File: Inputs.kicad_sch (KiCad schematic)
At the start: 12 parts, among them J7 Screw_Terminal_01x04, J8 Screw_Terminal_01x04, U10 LTV-247, U9 LTV-247

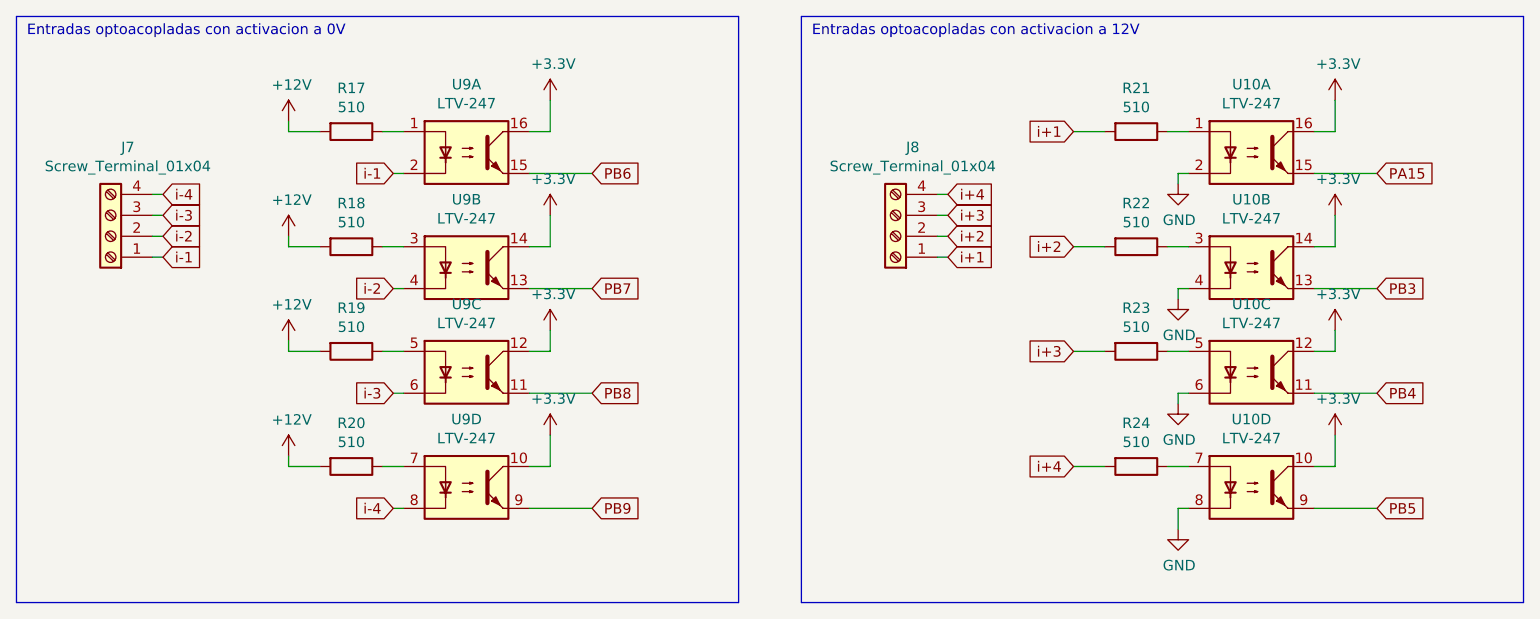
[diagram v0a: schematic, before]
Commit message: Planteamiento nuevo proeycto de mosquito - Se eelmiraon del esquematico las entradas a 0V y las salidas a Leds
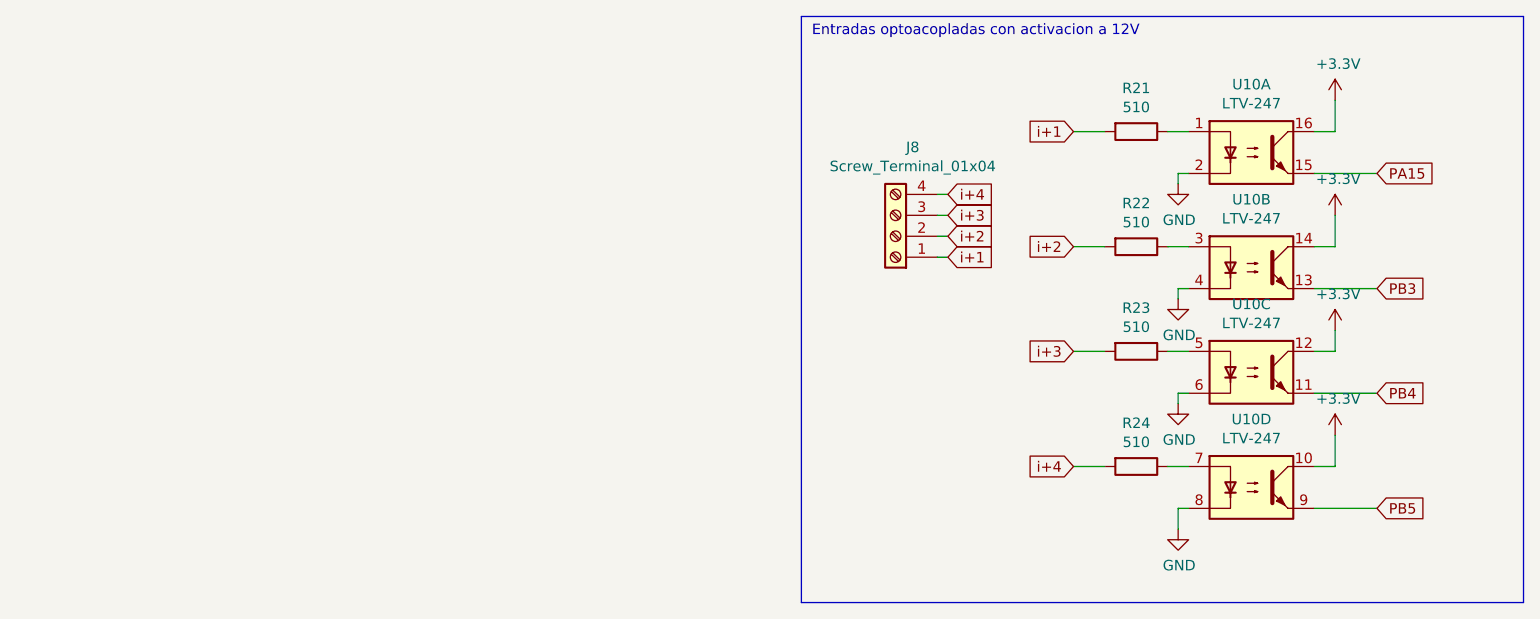
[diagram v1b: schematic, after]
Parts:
- removed J7: Screw_Terminal_01x04, Connector_Phoenix_MC_HighVoltage:PhoenixContact_MCV_1,5_4-G-5.08_1x04_P5.08mm_Vertical, symbol Connector:Screw_Terminal_01x04
- removed R17, R18, R19, R20: 510, Resistor_SMD:R_1210_3225Metric, symbol Device:R
- removed U9: LTV-247, Package_SO:SOP-16_4.4x10.4mm_P1.27mm, symbol Isolator:LTV-247
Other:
- note removed: "Entradas optoacopladas con activacion a 0V"
